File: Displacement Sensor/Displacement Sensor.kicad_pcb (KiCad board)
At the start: 2 copper layers, 56.8 x 46 mm, 25 parts, among them J1 DTF13-6P, U1 TJA1050DRG, U2 MCP2515-I, X1 8MHz

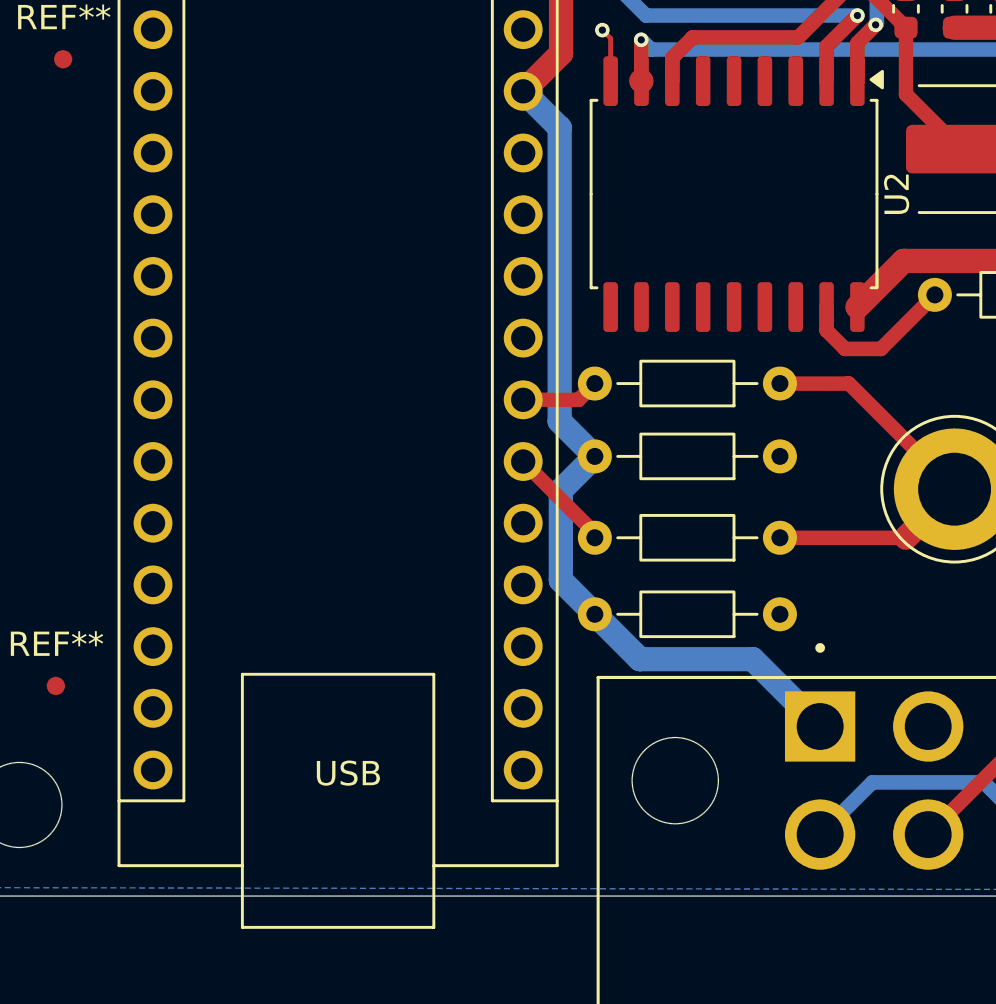
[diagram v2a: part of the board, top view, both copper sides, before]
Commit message: Added Interrupt
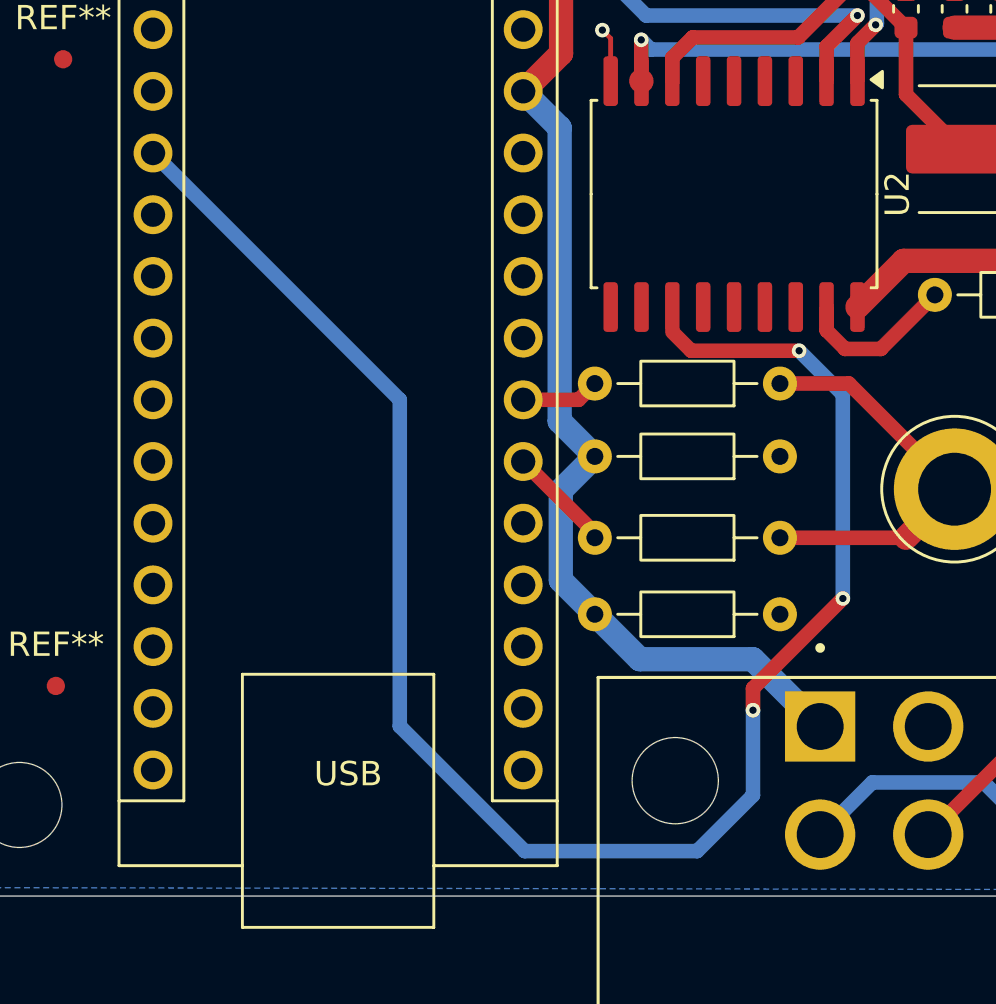
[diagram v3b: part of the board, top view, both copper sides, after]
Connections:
- A1 pad 5: unconnected-(A1-D2-Pad5) -> INT
- U2 pad 12: unconnected-(U2-~{INT}-Pad12) -> INT
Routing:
- net INT: track 0.00 -> 72.6 mm, vias 0 -> 3
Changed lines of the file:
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@@
 	(net 21 "unconnected-(A1-SCK-Pad16)")
 	(net 22 "unconnected-(A1-MOSI-Pad14)")
-	(net 23 "unconnected-(A1-D2-Pad5)")
+	(net 23 "INT")
 	(net 24 "Net-(A1-A2)")
 	(net 25 "unconnected-(A1-MISO-Pad15)")
@@
 	(net 42 "unconnected-(U2-~{RX1BF}-Pad10)")
 	(net 43 "SCK")
-	(net 44 "unconnected-(U2-~{INT}-Pad12)")
-	(net 45 "unconnected-(U2-~{TX1RTS}-Pad5)")
-	(net 46 "unconnected-(U2-CLKOUT{slash}SOF-Pad3)")
-	(net 47 "High")
-	(net 48 "Low")
-	(net 49 "unconnected-(U2-~{RX0BF}-Pad11)")
+	(net 44 "unconnected-(U2-~{TX1RTS}-Pad5)")
+	(net 45 "unconnected-(U2-CLKOUT{slash}SOF-Pad3)")
+	(net 46 "High")
+	(net 47 "Low")
+	(net 48 "unconnected-(U2-~{RX0BF}-Pad11)")
 	(footprint "Capacitor_SMD:C_0603_1608Metric"
 		(layer "F.Cu")
@@
 			(layers "F.Cu" "F.Mask" "F.Paste")
 			(roundrect_rratio 0.25)
-			(net 48 "Low")
+			(net 47 "Low")
 			(pinfunction "CANL")
 			(pintype "passive")
@@
 			(layers "F.Cu" "F.Mask" "F.Paste")
 			(roundrect_rratio 0.25)
-			(net 47 "High")
+			(net 46 "High")
 			(pinfunction "CANH")
 			(pintype "passive")
@@
 			(layers "F.Cu" "F.Mask" "F.Paste")
 			(roundrect_rratio 0.25)
-			(net 46 "unconnected-(U2-CLKOUT{slash}SOF-Pad3)")
+			(net 45 "unconnected-(U2-CLKOUT{slash}SOF-Pad3)")
 			(pinfunction "CLKOUT/SOF")
 			(pintype "passive+no_connect")
@@
 			(layers "F.Cu" "F.Mask" "F.Paste")
 			(roundrect_rratio 0.25)
-			(net 45 "unconnected-(U2-~{TX1RTS}-Pad5)")
+			(net 44 "unconnected-(U2-~{TX1RTS}-Pad5)")
 			(pinfunction "~{TX1RTS}")
 			(pintype "passive+no_connect")
@@
 			(layers "F.Cu" "F.Mask" "F.Paste")
 			(roundrect_rratio 0.25)
-			(net 49 "unconnected-(U2-~{RX0BF}-Pad11)")
+			(net 48 "unconnected-(U2-~{RX0BF}-Pad11)")
 			(pinfunction "~{RX0BF}")
 			(pintype "passive+no_connect")
@@
 			(layers "F.Cu" "F.Mask" "F.Paste")
 			(roundrect_rratio 0.25)
-			(net 44 "unconnected-(U2-~{INT}-Pad12)")
+			(net 23 "INT")
 			(pinfunction "~{INT}")
-			(pintype "passive+no_connect")
+			(pintype "passive")
 		)
 		(pad "13" smd roundrect
@@
 			(layers "*.Cu" "*.Mask")
 			(remove_unused_layers no)
-			(net 23 "unconnected-(A1-D2-Pad5)")
+			(net 23 "INT")
 			(pinfunction "D2")
 			(pintype "bidirectional")
@@
 			(layers "*.Cu" "*.Mask")
 			(remove_unused_layers no)
-			(net 48 "Low")
+			(net 47 "Low")
 			(pinfunction "3")
 			(pintype "passive")
@@
 			(layers "*.Cu" "*.Mask")
 			(remove_unused_layers no)
-			(net 47 "High")
+			(net 46 "High")
 			(pinfunction "4")
 			(pintype "passive")
@@
 			(layers "*.Cu" "*.Mask")
 			(remove_unused_layers no)
-			(net 48 "Low")
+			(net 47 "Low")
 			(pinfunction "5")
 			(pintype "passive")
@@
 			(layers "*.Cu" "*.Mask")
 			(remove_unused_layers no)
-			(net 47 "High")
+			(net 46 "High")
 			(pinfunction "6")
 			(pintype "passive")
@@
 	)
 	(segment
+		(start 96.7 117.1)
+		(end 96.7 116.2)
+		(width 0.6)
+		(layer "F.Cu")
+		(net 23)
+	)
+	(segment
+		(start 94.155001 102.3)
+		(end 93.38 101.524999)
+		(width 0.6)
+		(layer "F.Cu")
+		(net 23)
+	)
+	(segment
+		(start 96.7 116.2)
+		(end 100.4 112.5)
+		(width 0.6)
+		(layer "F.Cu")
+		(net 23)
+	)
+	(segment
+		(start 93.38 101.524999)
+		(end 93.38 100.5)
+		(width 0.2)
+		(layer "F.Cu")
+		(net 23)
+	)
+	(segment
+		(start 98.6 102.3)
+		(end 94.155001 102.3)
+		(width 0.6)
+		(layer "F.Cu")
+		(net 23)
+	)
+	(via
+		(at 96.7 117.1)
+		(size 0.6)
+		(drill 0.3)
+		(layers "F.Cu" "B.Cu")
+		(net 23)
+	)
+	(via
+		(at 100.4 112.5)
+		(size 0.6)
+		(drill 0.3)
+		(layers "F.Cu" "B.Cu")
+		(net 23)
+	)
+	(via
+		(at 98.6 102.3)
+		(size 0.6)
+		(drill 0.3)
+		(layers "F.Cu" "B.Cu")
+		(net 23)
+	)
+	(segment
+		(start 94.4 122.9)
+		(end 96.7 120.6)
+		(width 0.6)
+		(layer "B.Cu")
+		(net 23)
+	)
+	(segment
+		(start 82.159 117.759)
+		(end 87.3 122.9)
+		(width 0.6)
+		(layer "B.Cu")
+		(net 23)
+	)
+	(segment
+		(start 100.4 104.1)
+		(end 98.6 102.3)
+		(width 0.6)
+		(layer "B.Cu")
+		(net 23)
+	)
+	(segment
+		(start 96.7 120.6)
+		(end 96.7 117.1)
+		(width 0.6)
+		(layer "B.Cu")
+		(net 23)
+	)
+	(segment
+		(start 72 94.16)
+		(end 82.159 104.319)
+		(width 0.6)
+		(layer "B.Cu")
+		(net 23)
+	)
+	(segment
+		(start 87.3 122.9)
+		(end 94.4 122.9)
+		(width 0.6)
+		(layer "B.Cu")
+		(net 23)
+	)
+	(segment
+		(start 100.4 112.5)
+		(end 100.4 104.1)
+		(width 0.6)
+		(layer "B.Cu")
+		(net 23)
+	)
+	(segment
+		(start 82.159 104.319)
+		(end 82.159 117.759)
+		(width 0.6)
+		(layer "B.Cu")
+		(net 23)
+	)
+	(segment
 		(start 90.19 110)
 		(end 90.19 109.81)
@@
 		(width 0.6)
 		(layer "F.Cu")
-		(net 47)
+		(net 46)
 	)
 	(segment
@@
 		(width 0.6)
 		(layer "F.Cu")
-		(net 47)
+		(net 46)
 	)
 	(segment
@@
 		(width 0.6)
 		(layer "F.Cu")
-		(net 47)
+		(net 46)
 	)
 	(via
@@
 		(drill 0.3)
 		(layers "F.Cu" "B.Cu")
-		(net 47)
+		(net 46)
 	)
 	(segment
@@
 		(width 0.6)
 		(layer "B.Cu")
-		(net 47)
+		(net 46)
 	)
 	(segment
@@
 		(width 0.6)
 		(layer "B.Cu")
-		(net 47)
+		(net 46)
 	)
 	(segment
@@
 		(width 0.6)
 		(layer "B.Cu")
-		(net 47)
+		(net 46)
 	)
 	(segment
@@
 		(width 0.6)
 		(layer "B.Cu")
-		(net 47)
+		(net 46)
 	)
 	(segment
@@
 		(width 0.6)
 		(layer "B.Cu")
-		(net 47)
+		(net 46)
 	)
 	(segment
@@
 		(width 0.6)
 		(layer "B.Cu")
-		(net 47)
+		(net 46)
 	)
 	(segment
@@
 		(width 0.6)
 		(layer "B.Cu")
-		(net 47)
+		(net 46)
 	)
 	(segment
@@
 		(width 0.6)
 		(layer "B.Cu")
-		(net 47)
+		(net 46)
 	)
 	(segment
@@
 		(width 0.6)
 		(layer "B.Cu")
-		(net 47)
+		(net 46)
 	)
 	(segment
@@
 		(width 0.6)
 		(layer "F.Cu")
-		(net 48)
+		(net 47)
 	)
 	(segment
@@
 		(width 0.6)
 		(layer "F.Cu")
-		(net 48)
+		(net 47)
 	)
 	(segment
@@
 		(width 0.6)
 		(layer "F.Cu")
-		(net 48)
+		(net 47)
 	)
 	(segment
@@
 		(width 0.6)
 		(layer "F.Cu")
-		(net 48)
+		(net 47)
 	)
 	(segment
@@
 		(width 0.6)
 		(layer "F.Cu")
-		(net 48)
+		(net 47)
 	)
 	(segment
@@
 		(width 0.6)
 		(layer "F.Cu")
-		(net 48)
+		(net 47)
 	)
 	(segment
@@
 		(width 1)
 		(layer "F.Cu")
-		(net 48)
+		(net 47)
 	)
 	(segment
@@
 		(width 0.6)
 		(layer "F.Cu")
-		(net 48)
+		(net 47)
 	)
 	(segment
@@
 		(width 0.6)
 		(layer "F.Cu")
-		(net 48)
+		(net 47)
 	)
 	(via
@@
 		(drill 0.3)
 		(layers "F.Cu" "B.Cu")
-		(net 48)
+		(net 47)
 	)
 	(via
@@
 		(drill 0.3)
 		(layers "F.Cu" "B.Cu")
-		(net 48)
+		(net 47)
 	)
 	(segment
@@
 		(width 0.6)
 		(layer "B.Cu")
-		(net 48)
+		(net 47)
 	)
 	(segment
@@
 		(width 0.6)
 		(layer "B.Cu")
-		(net 48)
+		(net 47)
 	)
 	(segment
@@
 		(width 0.6)
 		(layer "B.Cu")
-		(net 48)
+		(net 47)
 	)
 	(zone

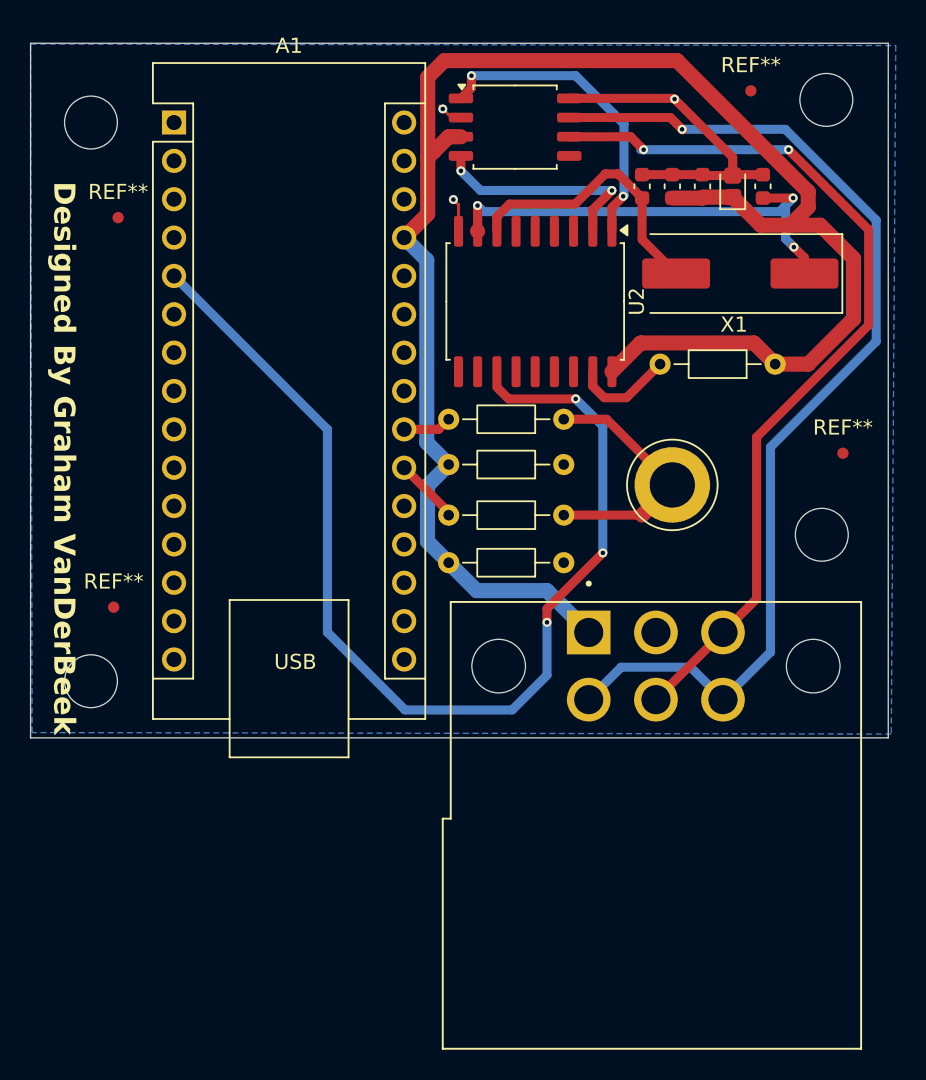
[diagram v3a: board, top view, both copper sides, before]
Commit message: Connected Can Bus to Arduino
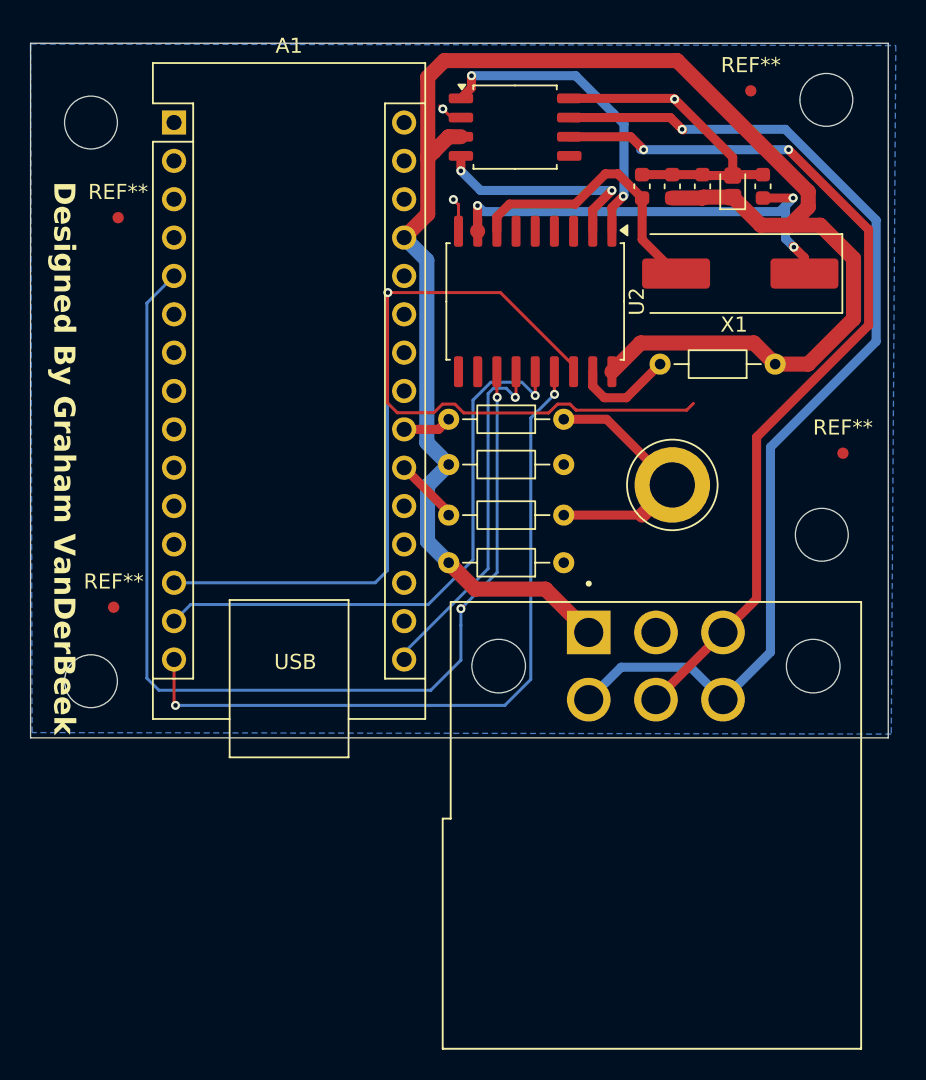
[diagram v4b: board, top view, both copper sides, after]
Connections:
- A1 pad 13: unconnected-(A1-D10-Pad13) -> CS
- A1 pad 14: unconnected-(A1-MOSI-Pad14) -> SI
- A1 pad 15: unconnected-(A1-MISO-Pad15) -> SO
- A1 pad 16: unconnected-(A1-SCK-Pad16) -> SCK
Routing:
- net CS: track 0.00 -> 76.5 mm, vias 0 -> 1
- net SO: track 0.00 -> 48.4 mm, vias 0 -> 2
- net SI: track 0.00 -> 38.6 mm, vias 0 -> 1
- net SCK: track 0.00 -> 23.8 mm, vias 0 -> 1
- net INT: track 72.6 -> 70.1 mm, vias 3 -> 2

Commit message: AAAAAAAAAA
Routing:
- net CS: track 76.5 -> 47.6 mm
- net INT: track 70.1 -> 69.8 mm, vias 2 -> 1
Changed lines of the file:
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@@
-	)
-	(segment
-		(start 91.1785 116.0215)
-		(end 91 116.2)
-		(width 0.2)
-		(layer "F.Cu")
-		(net 22)
 	)
 	(segment
@@
 		(width 0.2)
 		(layer "F.Cu")
-		(net 22)
-	)
-	(via
-		(at 91 116.2)
-		(size 0.6)
-		(drill 0.3)
-		(layers "F.Cu" "B.Cu")
 		(net 22)
 	)
@@
 	)
 	(segment
-		(start 91.191 103.235372)
-		(end 96.809 103.235372)
-		(width 0.2)
-		(layer "F.Cu")
-		(net 36)
-	)
-	(segment
-		(start 89.205372 103.219)
-		(end 89.775372 102.649)
-		(width 0.2)
-		(layer "F.Cu")
-		(net 36)
-	)
-	(segment
-		(start 86.78395 103.219)
-		(end 89.205372 103.219)
-		(width 0.2)
-		(layer "F.Cu")
-		(net 36)
-	)
-	(segment
-		(start 86.139 95.283)
-		(end 86.139 102.57405)
-		(width 0.2)
-		(layer "F.Cu")
-		(net 36)
-	)
-	(segment
-		(start 90.604628 102.649)
-		(end 91.191 103.235372)
-		(width 0.2)
-		(layer "F.Cu")
-		(net 36)
-	)
-	(segment
-		(start 97.395372 102.649)
-		(end 98.224628 102.649)
-		(width 0.2)
-		(layer "F.Cu")
-		(net 36)
-	)
-	(segment
 		(start 98.46 100.103032)
 		(end 93.617968 95.261)
@@
 	)
 	(segment
-		(start 98.224628 102.649)
-		(end 98.624628 103.049)
-		(width 0.2)
-		(layer "F.Cu")
-		(net 36)
-	)
-	(segment
-		(start 86.139 102.57405)
-		(end 86.78395 103.219)
-		(width 0.2)
-		(layer "F.Cu")
-		(net 36)
-	)
-	(segment
-		(start 89.775372 102.649)
-		(end 90.604628 102.649)
-		(width 0.2)
-		(layer "F.Cu")
-		(net 36)
-	)
-	(segment
-		(start 98.624628 103.049)
-		(end 105.951 103.049)
-		(width 0.2)
-		(layer "F.Cu")
-		(net 36)
-	)
-	(segment
 		(start 98.46 100.5)
 		(end 98.46 100.103032)
@@
 	)
 	(segment
-		(start 105.951 103.049)
-		(end 106.4 102.6)
-		(width 0.2)
-		(layer "F.Cu")
-		(net 36)
-	)
-	(segment
 		(start 86.161 95.261)
 		(end 86.139 95.283)
 		(width 0.2)
 		(layer "F.Cu")
-		(net 36)
-	)
-	(segment
-		(start 96.809 103.235372)
-		(end 97.395372 102.649)
-		(width 0.2)
-		(layer "F.Cu")
